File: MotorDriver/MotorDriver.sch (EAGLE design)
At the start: 17 parts, among them U1 ATTINY841, U2 NJM2670

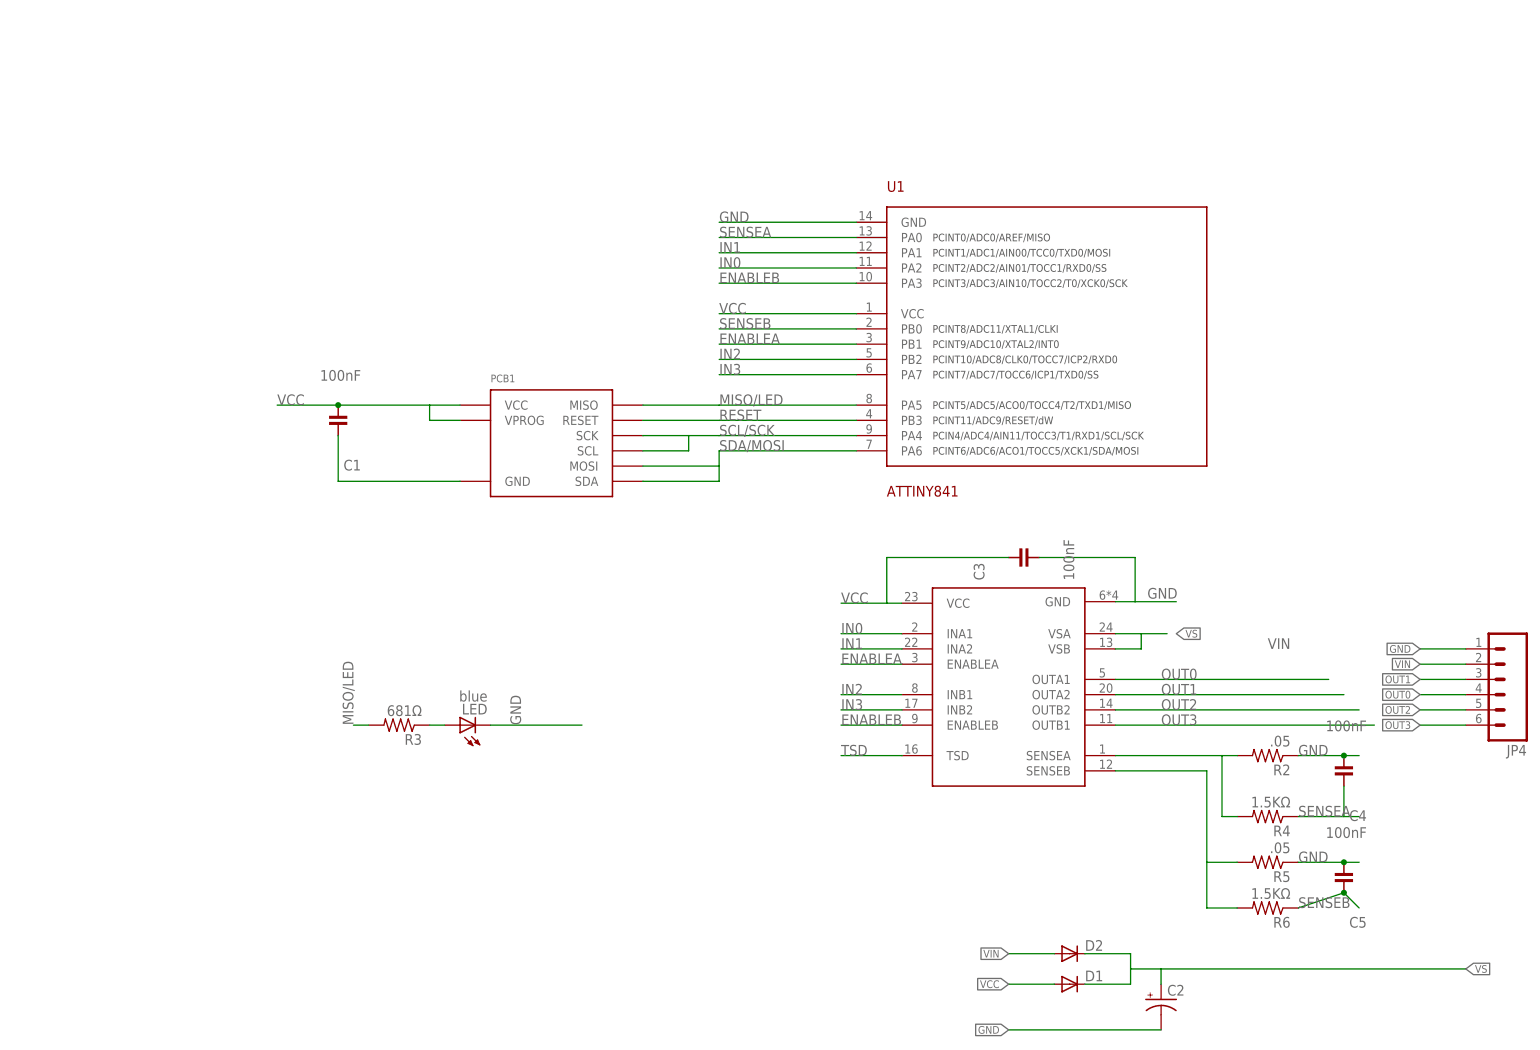
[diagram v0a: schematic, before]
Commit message: Major revision of all boards. Cleaned up old files. Exported BOM csv files for all boards
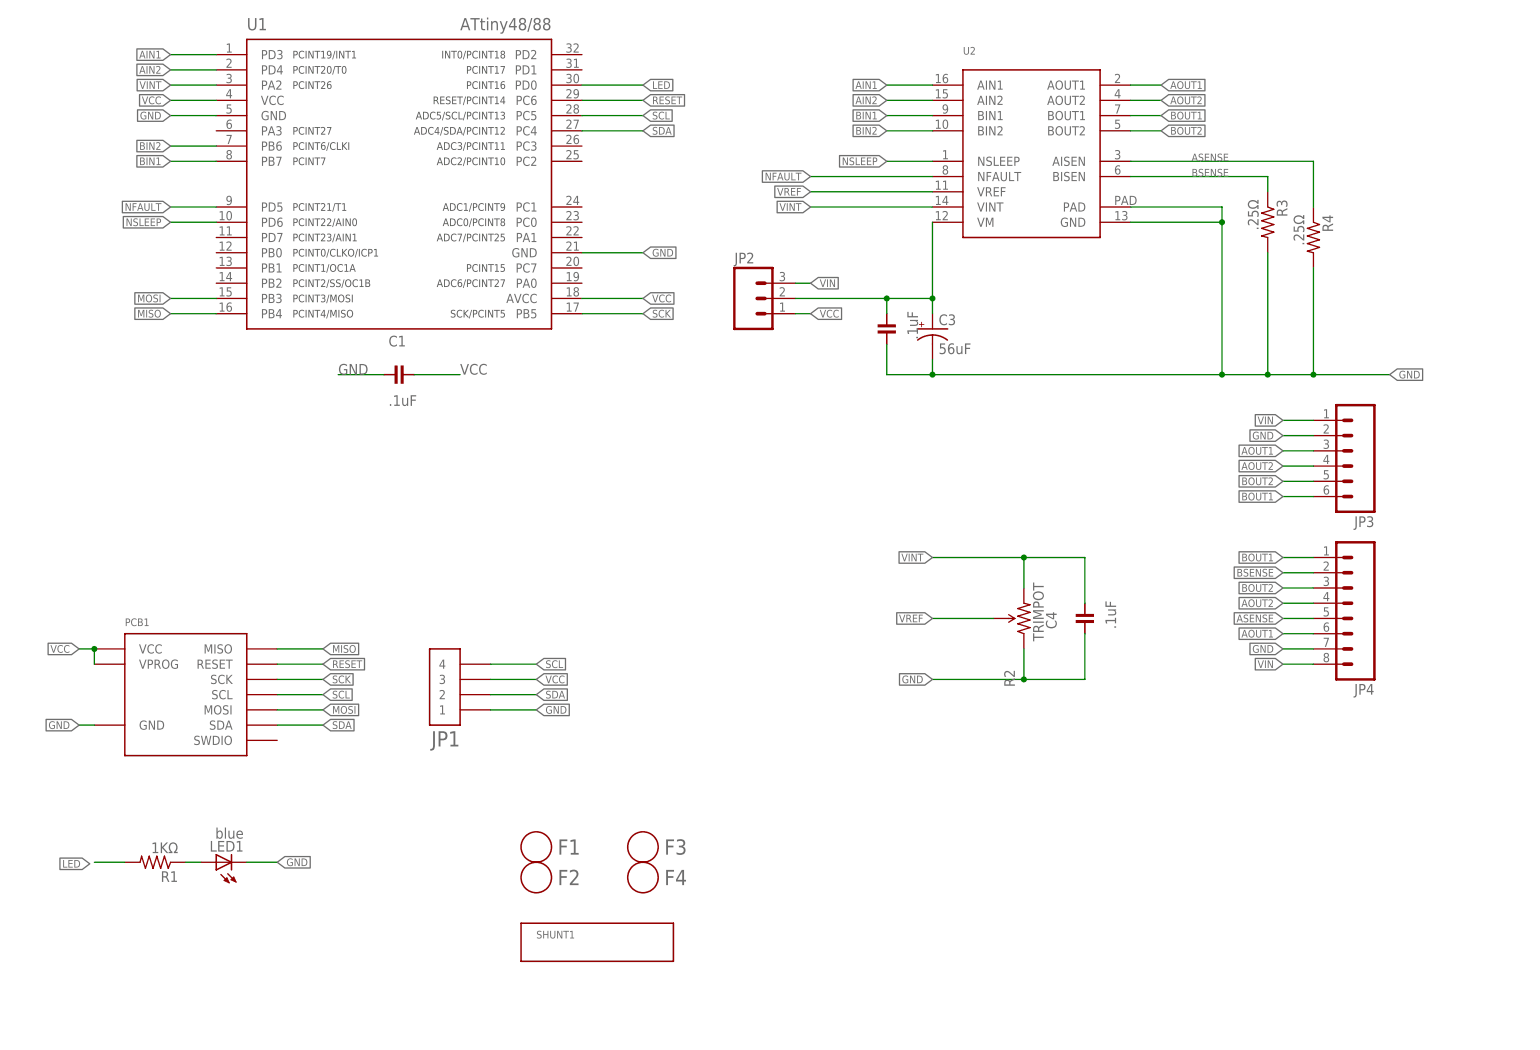
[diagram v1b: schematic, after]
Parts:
- removed C5: 100nF, Modulo:CAPACITOR-100NF
- removed D1, D2: (no value), SparkFun-DiscreteSemi:DIODESMA
- removed LED: blue, Modulo:LED-0805-BLUE
- removed R5: .05, Modulo:RESISTOR
- removed R6: 1.5KΩ, Modulo:RESISTOR-1.5KΩ
- added F1, F2, F3, F4: FIDUCIAL, Modulo:FIDUCIAL
- added JP1: HEADER-1X4-AMPMODU, Modulo:HEADER-1X4-AMPMODU
- added JP2: (no value), SparkFun-Connectors:M03LOCK_NO_SILK
- added JP3: (no value), SparkFun-Connectors:M063.5MM-6
- added LED1: blue, Modulo:LED-0805-BLUE
- added R1: 1KΩ, Modulo:RESISTOR-1KΩ
- C1, C4: value 100nF -> .1uF; device Modulo:CAPACITOR-100NF -> Modulo:CAPACITOR-.1UF
- C2: value (none) -> .1uF; device SparkFun-Capacitors:CAP_POLC -> Modulo:CAPACITOR-.1UF; PARTNUM EEE-0JA101WR -> (none); RATING (none) -> >20V
- C3: value 100nF -> 56uF; device Modulo:CAPACITOR-100NF -> Modulo:CAPACITOR-POL-56UF-25V; RATING (none) -> >20V
- JP4: device SparkFun-Connectors:M063.5MM-6 -> SparkFun-Connectors:M08NO_SILK; PARTNUM OSTTE060104 -> (none)
- PCB1: value DEVICE-PCB-TABS -> DEVICE-PCB; device Modulo:DEVICE-PCB-TABS -> Modulo:DEVICE-PCB; PARTNUM (none) -> Motor Driver PCB
- R2: value .05 -> TRIMPOT; device Modulo:RESISTOR -> Modulo:TRIMPOT; PARTNUM CSR0805FKR500 -> PVZ3A103C01R00
- R3: value 681Ω -> .25Ω; device Modulo:RESISTOR-681Ω -> SparkFun-Resistors:RESISTOR2010; PARTNUM (none) -> CSRN2010FKR250
- R4: value 1.5KΩ -> .25Ω; device Modulo:RESISTOR-1.5KΩ -> SparkFun-Resistors:RESISTOR2010; PARTNUM (none) -> CSRN2010FKR250
- U1: value ATTINY841 -> ATTINY48/88-TQFP; device Modulo:ATTINY841 -> Modulo:ATTINY48/88-TQFP
- U2: value NJM2670 -> DRV8848; device IntegerLabs:NJM2670 -> Modulo:DRV8848; PARTNUM NJM2670E3 -> DRV8848
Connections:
- removed net ENABLEA: U1.PB1, U2.ENABLEA
- removed net ENABLEB: U1.PA3, U2.ENABLEB
- removed net IN0: U1.PA2, U2.INA1
- removed net IN1: U1.PA1, U2.INA2
- removed net IN2: U1.PB2, U2.INB1
- removed net IN3: U1.PA7, U2.INB2
- removed net MISO/LED: PCB1.MISO, R3.2, U1.PA5
- removed net N$2: R2.2, R4.2, U2.SENSEA
- removed net N$3: R5.2, R6.2, U2.SENSEB
- removed net N$5: LED.A, R3.1
- removed net OUT0: JP4.4, U2.OUTA1
- removed net OUT1: JP4.3, U2.OUTA2
- removed net OUT2: JP4.5, U2.OUTB2
- removed net OUT3: JP4.6, U2.OUTB1
- removed net SCL/SCK: PCB1.SCK, PCB1.SCL, U1.PA4
- removed net SDA/MOSI: PCB1.MOSI, PCB1.SDA, U1.PA6
- removed net SENSEA: C4.1, R4.1, U1.PA0
- removed net SENSEB: C5.1, R6.1, U1.PB0
- removed net TSD: U2.TSD
- removed net VS: C2.+, D1.C, D2.C, U2.VSA, U2.VSB
- new net AIN1: U1.PD3, U2.AIN1
- new net AIN2: U1.PD4, U2.AIN2
- new net AOUT1: JP3.3, JP4.6, U2.AOUT1
- new net AOUT2: JP3.4, JP4.4, U2.AOUT2
- new net ASENSE: JP4.5, R4.1, U2.AISEN
- new net BIN1: U1.PB7, U2.BIN1
- new net BIN2: U1.PB6, U2.BIN2
- new net BOUT1: JP3.6, JP4.1, U2.BOUT1
- new net BOUT2: JP3.5, JP4.3, U2.BOUT2
- new net BSENSE: JP4.2, R3.1, U2.BISEN
- new net LED: R1.2, U1.PD0
- new net MISO: PCB1.MISO, U1.PB4
- new net MOSI: PCB1.MOSI, U1.PB3
- new net N$10: C2.1, C3.+, JP2.2, U2.VM
- new net N$7: LED1.A, R1.1
- new net NFAULT: U1.PD5, U2.NFAULT
- new net NSLEEP: U1.PD6, U2.NSLEEP
- new net SCK: PCB1.SCK, U1.PB5
- new net SCL: JP1.4, PCB1.SCL, U1.PC5
- new net SDA: JP1.2, PCB1.SDA, U1.PC4
- new net VINT: C4.1, R2.CW, U1.PA2, U2.VINT
- new net VREF: R2.WIPER, U2.VREF
- net GND: now also C1.2, C2.2, C3.-, JP1.1, JP3.2, JP4.7, LED1.C, R2.CCW, R3.2, R4.2, U1.GND@1, U2.PAD; no longer C1.1, C2.-, C3.2, C5.2, JP4.1, LED.C, R2.1, R5.1
- net RESET: now also U1.PC6; no longer U1.PB3
- net VCC: now also C1.1, JP1.3, JP2.1, U1.AVCC; no longer C1.2, C3.1, D1.A, U2.VCC
- net VIN: now also JP2.3, JP3.1, JP4.8; no longer D2.A, JP4.2
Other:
- moved on the sheet: C1, C4, R3, R4

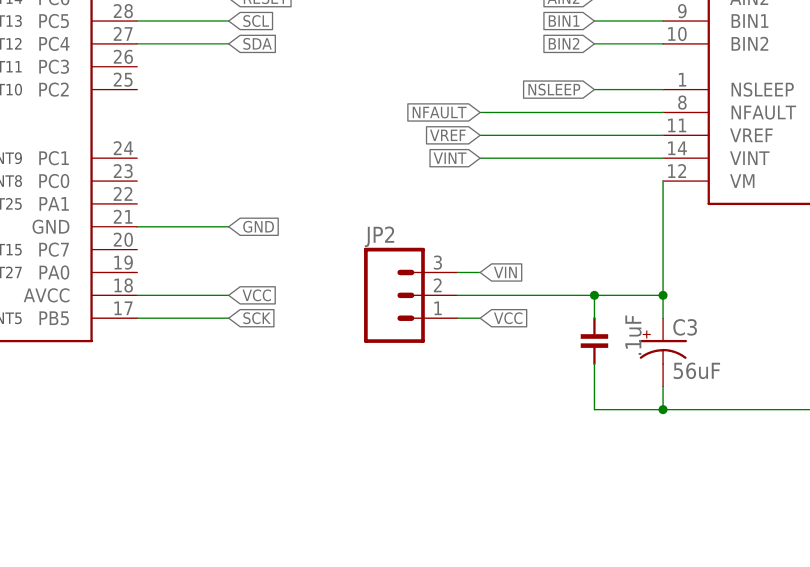
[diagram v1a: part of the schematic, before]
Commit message: New diode selections
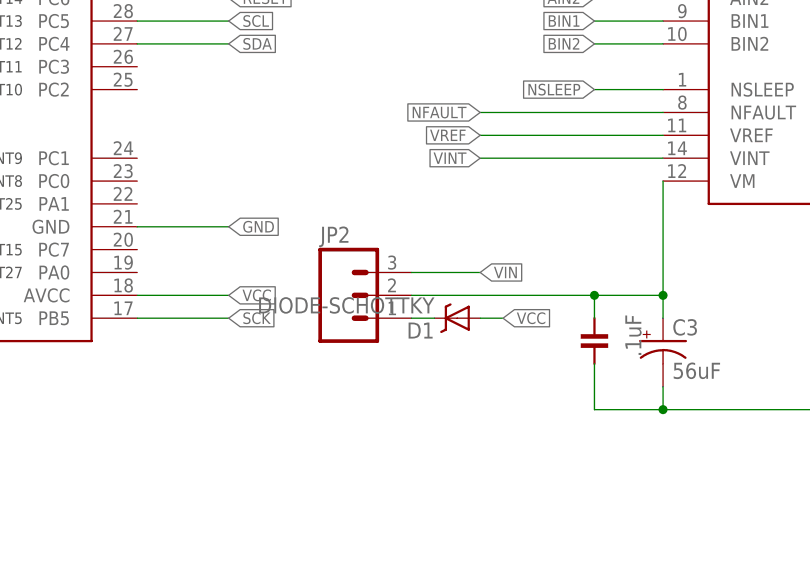
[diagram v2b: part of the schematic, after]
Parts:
- added D1: DIODE-SCHOTTKY, Modulo:DIODE-SCHOTTKY
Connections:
- new net N$1: D1.C, JP2.1
- net VCC: now also D1.A; no longer JP2.1
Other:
- moved on the sheet: JP2
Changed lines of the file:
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@@
 </part>
 <part name="JP4" library="SparkFun-Connectors" deviceset="M08" device="NO_SILK"/>
+<part name="D1" library="Modulo" deviceset="DIODE-SCHOTTKY" device="" value="DIODE-SCHOTTKY"/>
 </parts>
 <sheets>
@@
 <attribute name="RATING" x="144.78" y="116.84" size="1.778" layer="96" display="off"/>
 </instance>
-<instance part="JP2" gate="G$1" x="121.92" y="121.92">
-<attribute name="PARTNUM" x="121.92" y="121.92" size="1.27" layer="96" display="off"/>
+<instance part="JP2" gate="G$1" x="116.84" y="121.92">
+<attribute name="PARTNUM" x="116.84" y="121.92" size="1.27" layer="96" display="off"/>
 </instance>
 <instance part="SHUNT1" gate="G$1" x="88.9" y="12.7">
@@
 </instance>
 <instance part="JP4" gate="G$1" x="220.98" y="71.12" rot="R180"/>
+<instance part="D1" gate="G$1" x="129.54" y="119.38" rot="R180"/>
 </instances>
 <busses>
@@
 <wire x1="78.74" y1="58.42" x2="86.36" y2="58.42" width="0.1524" layer="91"/>
 <label x="86.36" y="58.42" size="1.27" layer="95" xref="yes"/>
-</segment>
-<segment>
-<wire x1="129.54" y1="119.38" x2="132.08" y2="119.38" width="0.1524" layer="91"/>
-<label x="132.08" y="119.38" size="1.27" layer="95" xref="yes"/>
-<pinref part="JP2" gate="G$1" pin="1"/>
 </segment>
 <segment>
@@
 <label x="10.16" y="63.5" size="1.27" layer="95" rot="R180" xref="yes"/>
 <junction x="12.7" y="63.5"/>
+</segment>
+<segment>
+<pinref part="D1" gate="G$1" pin="A"/>
+<wire x1="132.08" y1="119.38" x2="134.62" y2="119.38" width="0.1524" layer="91"/>
+<label x="134.62" y="119.38" size="1.27" layer="95" xref="yes"/>
 </segment>
 </net>
@@
 <wire x1="144.78" y1="119.38" x2="144.78" y2="121.92" width="0.1524" layer="91"/>
 <pinref part="JP2" gate="G$1" pin="2"/>
-<wire x1="129.54" y1="121.92" x2="144.78" y2="121.92" width="0.1524" layer="91"/>
+<wire x1="124.46" y1="121.92" x2="144.78" y2="121.92" width="0.1524" layer="91"/>
 <junction x="144.78" y="121.92"/>
 </segment>
@@
 <net name="VIN" class="0">
 <segment>
-<wire x1="129.54" y1="124.46" x2="132.08" y2="124.46" width="0.1524" layer="91"/>
+<wire x1="124.46" y1="124.46" x2="132.08" y2="124.46" width="0.1524" layer="91"/>
 <label x="132.08" y="124.46" size="1.27" layer="95" xref="yes"/>
 <pinref part="JP2" gate="G$1" pin="3"/>
@@
 </segment>
 </net>
+<net name="N$1" class="0">
+<segment>
+<pinref part="JP2" gate="G$1" pin="1"/>
+<pinref part="D1" gate="G$1" pin="C"/>
+<wire x1="124.46" y1="119.38" x2="127" y2="119.38" width="0.1524" layer="91"/>
+</segment>
+</net>
